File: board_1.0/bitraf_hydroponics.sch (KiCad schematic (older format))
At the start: 40 parts, among them P1 12V_PWR, P10 I2C_4, P11 BUZZ, P12 LDR, P13 TEMP_HUM, P14 PROGRAMMER, P15 LCD, P16 Radio_433, P2 SWITCH_1, P3 SWITCH_2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

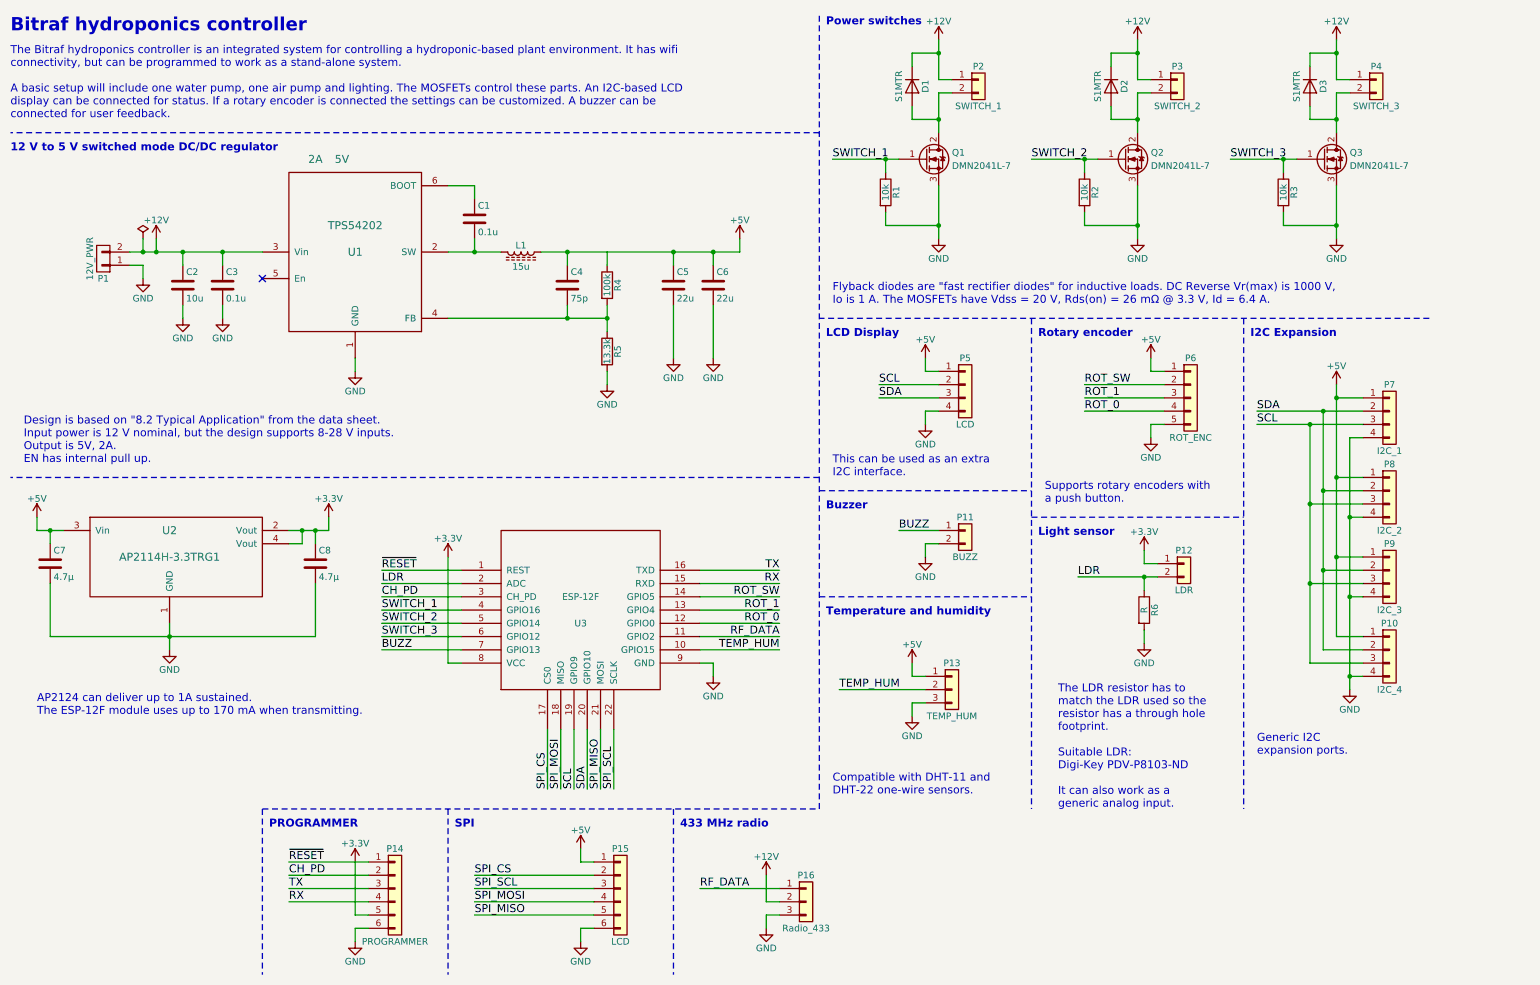
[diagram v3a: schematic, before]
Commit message: schematic: o Changing 12V connector to the same as the rest. o Better label for Radio. o Changing R6 from SMD to THT so it is easier to customize with the LDR. pcb: o Adding copper zones connected to GND on front and back. o Expanding board to 50x100 mm. Moving all connectors onto board.
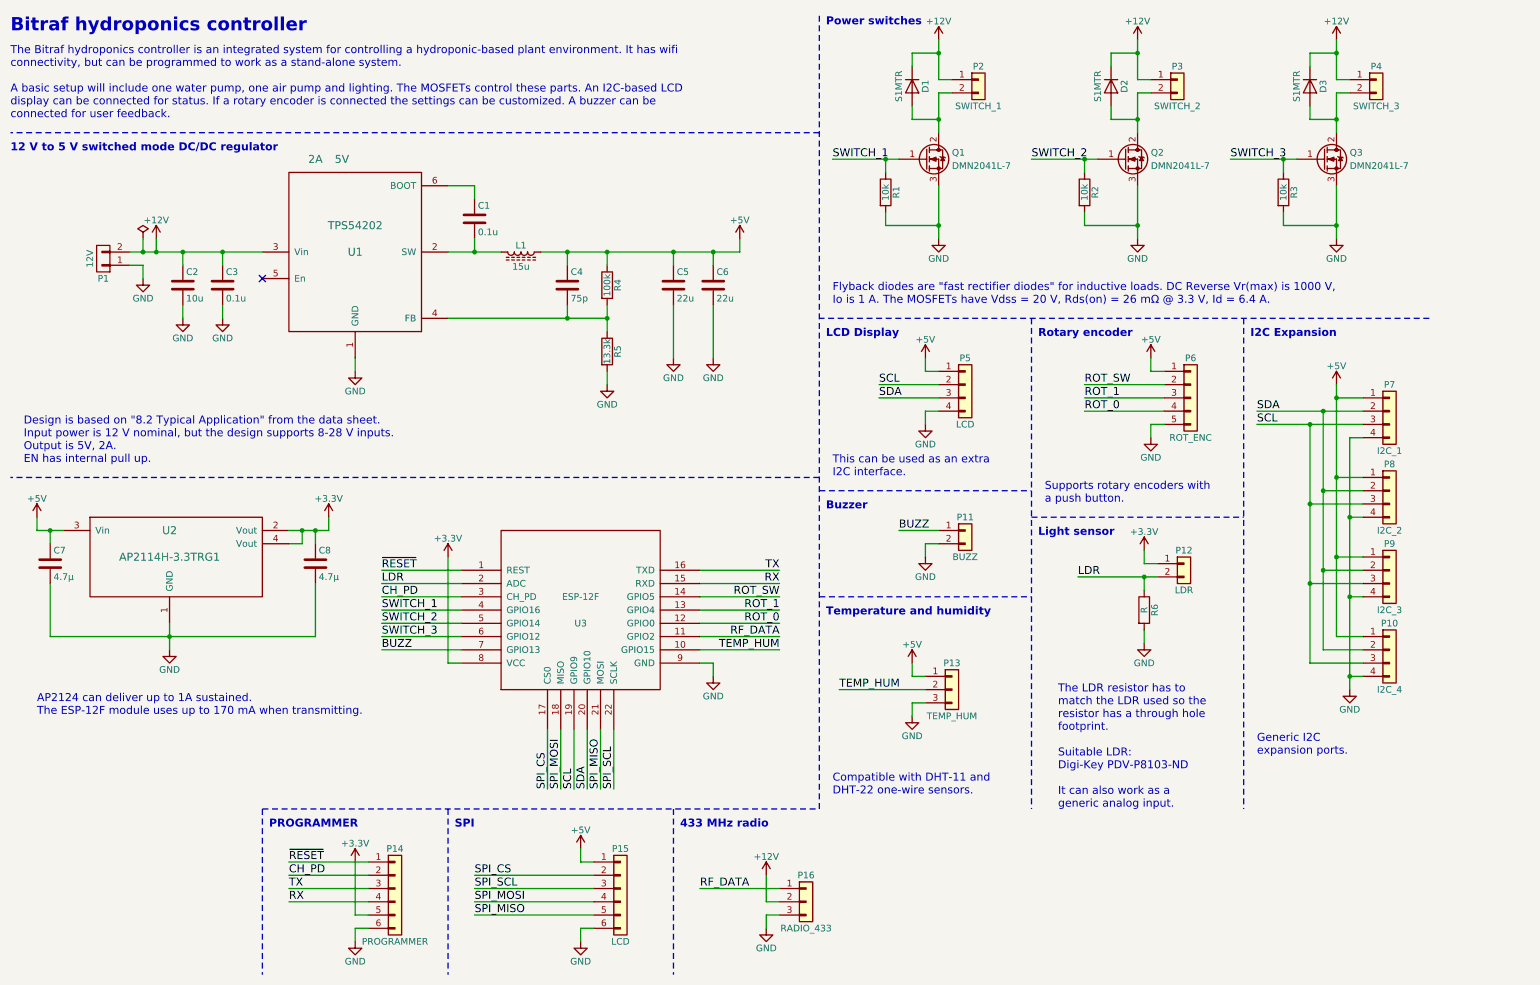
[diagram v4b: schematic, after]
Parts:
- P1: value 12V_PWR -> 12V; footprint Connectors_Terminal_Blocks:TerminalBlock_Pheonix_PT-3.5mm_2pol -> Connectors_Phoenix:PhoenixContact_PTSM0,5_4-HV-2,5_SMD
- P16: value Radio_433 -> RADIO_433
- R6: footprint Resistors_SMD:R_0805 -> Resistors_THT:R_Axial_DIN0207_L6.3mm_D2.5mm_P10.16mm_Horizontal
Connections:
- net +5V: now also R4.1
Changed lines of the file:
@@
 P 6500 7200
 F 0 "P16" H 6500 7400 50  0000 C CNN
-F 1 "Radio_433" H 6500 7000 50  0000 C CNN
+F 1 "RADIO_433" H 6500 7000 50  0000 C CNN
 F 2 "Socket_Strips:Socket_Strip_Straight_1x03_Pitch2.54mm" H 6500 7200 50  0001 C CNN
 F 3 "" H 6500 7200 50  0001 C CNN
@@
 P 1200 2350
 F 0 "P1" H 1200 2500 50  0000 C CNN
-F 1 "12V_PWR" V 1300 2350 50  0000 C CNN
-F 2 "Connectors_Terminal_Blocks:TerminalBlock_Pheonix_PT-3.5mm_2pol" H 1200 2350 50  0001 C CNN
+F 1 "12V" V 1300 2350 50  0000 C CNN
+F 2 "Connectors_Phoenix:PhoenixContact_PTSM0,5_4-HV-2,5_SMD" H 1200 2350 50  0001 C CNN
 F 3 "" H 1200 2350 50  0000 C CNN
 	1    1200 2350
@@
 F 0 "R6" V 9130 5000 50  0000 C CNN
 F 1 "R" V 9050 5000 50  0000 C CNN
-F 2 "Resistors_SMD:R_0805" V 8980 5000 50  0001 C CNN
+F 2 "Resistors_THT:R_Axial_DIN0207_L6.3mm_D2.5mm_P10.16mm_Horizontal" V 8980 5000 50  0001 C CNN
 F 3 "" H 9050 5000 50  0000 C CNN
 	1    9050 5000
@@
 	0    1    1    0
 $EndComp
+Connection ~ 5000 2300
 $EndSCHEMATC

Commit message: switched position on SDA and SCL on the LCD header to match the rest of I2C bus
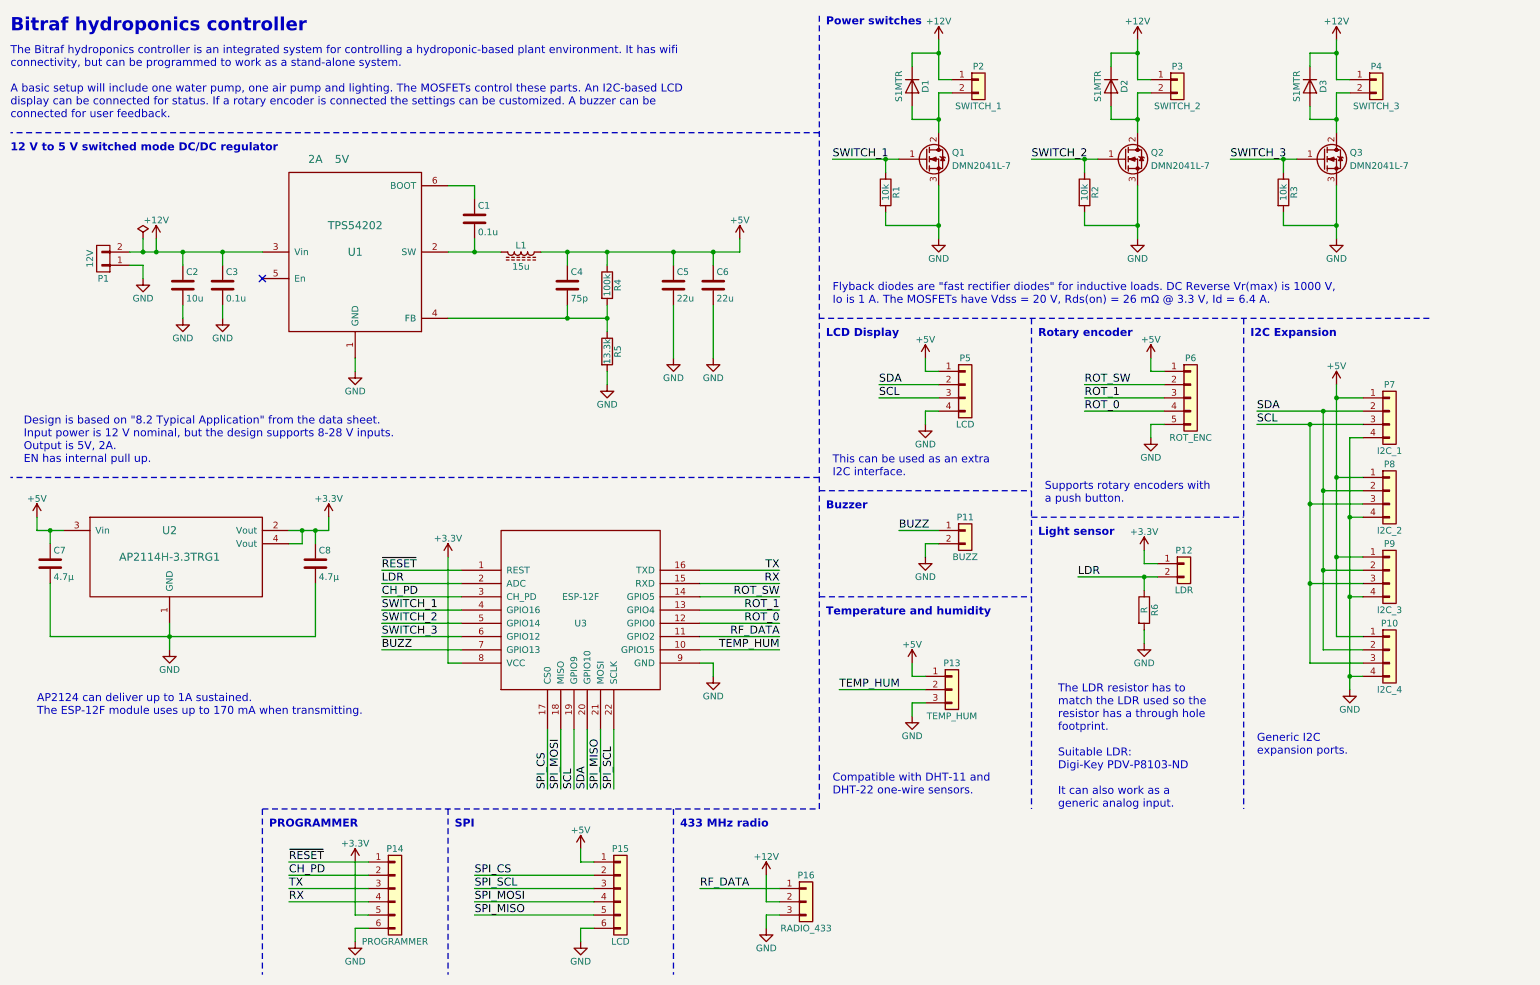
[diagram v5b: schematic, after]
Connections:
- net SCL: now also P5.3 (Pin_3); no longer P5.2 (Pin_2)
- net SDA: now also P5.2 (Pin_2); no longer P5.3 (Pin_3)
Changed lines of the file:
@@
 LIBS:nodemcu
 LIBS:tps54202
-LIBS:ESP8266
 LIBS:ap2114
 LIBS:bitraf_hydroponics-cache
@@
 	1    0    0    -1
 $EndComp
+Text Label 7050 3400 0    60   ~ 0
+SCL
 Text Label 7050 3300 0    60   ~ 0
-SCL
-Text Label 7050 3400 0    60   ~ 0
 SDA
 $Comp
@@
 	7600 1100 7500 1100
 Wire Wire Line
-	7500 1100 7500 1400
+	7500 1100 7500 1300
+Wire Wire Line
+	7500 1300 7500 1400
 Wire Wire Line
 	7500 1000 7600 1000
 Wire Wire Line
-	7500 700  7500 1000
+	7500 700  7500 800
+Wire Wire Line
+	7500 800  7500 1000
 Wire Wire Line
 	7300 1200 7300 1300
@@
 Connection ~ 7500 800
 Wire Wire Line
-	7500 1800 7500 2200
-Wire Wire Line
-	6700 1600 7200 1600
+	7500 1800 7500 2100
+Wire Wire Line
+	7500 2100 7500 2200
+Wire Wire Line
+	6700 1600 7100 1600
+Wire Wire Line
+	7100 1600 7200 1600
 Wire Wire Line
 	7100 1700 7100 1600
@@
 	9100 1100 9000 1100
 Wire Wire Line
-	9000 1100 9000 1400
+	9000 1100 9000 1300
+Wire Wire Line
+	9000 1300 9000 1400
 Wire Wire Line
 	9000 1000 9100 1000
 Wire Wire Line
-	9000 700  9000 1000
+	9000 700  9000 800
+Wire Wire Line
+	9000 800  9000 1000
 Wire Wire Line
 	8800 1200 8800 1300
@@
 Connection ~ 9000 800
 Wire Wire Line
-	9000 1800 9000 2200
-Wire Wire Line
-	8200 1600 8700 1600
+	9000 1800 9000 2100
+Wire Wire Line
+	9000 2100 9000 2200
+Wire Wire Line
+	8200 1600 8600 1600
+Wire Wire Line
+	8600 1600 8700 1600
 Wire Wire Line
 	8600 1700 8600 1600
@@
 	10600 1100 10500 1100
 Wire Wire Line
-	10500 1100 10500 1400
+	10500 1100 10500 1300
+Wire Wire Line
+	10500 1300 10500 1400
 Wire Wire Line
 	10500 1000 10600 1000
 Wire Wire Line
-	10500 700  10500 1000
+	10500 700  10500 800
+Wire Wire Line
+	10500 800  10500 1000
 Wire Wire Line
 	10300 1200 10300 1300
@@
 	10300 900  10300 800
 Wire Wire Line
-	10500 1800 10500 2200
-Wire Wire Line
-	9700 1600 10200 1600
+	10500 1800 10500 2100
+Wire Wire Line
+	10500 2100 10500 2200
+Wire Wire Line
+	9700 1600 10100 1600
+Wire Wire Line
+	10100 1600 10200 1600
 Wire Wire Line
 	10100 1700 10100 1600
@@
 	9200 3500 8600 3500
 Wire Wire Line
-	1400 2300 2400 2300
+	1400 2300 1500 2300
+Wire Wire Line
+	1500 2300 1600 2300
+Wire Wire Line
+	1600 2300 1800 2300
+Wire Wire Line
+	1800 2300 2100 2300
+Wire Wire Line
+	2100 2300 2400 2300
 Wire Wire Line
 	1600 2300 1600 2200
@@
 	7500 4400 7200 4400
 Wire Wire Line
-	8550 4750 9150 4750
+	8550 4750 9050 4750
+Wire Wire Line
+	9050 4750 9150 4750
 Wire Wire Line
 	9050 4750 9050 4850
@@
 	10400 5300 10700 5300
 Wire Wire Line
-	10500 3300 10500 5200
+	10500 3300 10500 3400
+Wire Wire Line
+	10500 3400 10500 4000
+Wire Wire Line
+	10500 4000 10500 4600
+Wire Wire Line
+	10500 4600 10500 5200
 Wire Wire Line
 	10600 5500 10700 5500
@@
 	10400 4100 10700 4100
 Wire Wire Line
-	9900 3600 10700 3600
-Wire Wire Line
-	9900 3500 10700 3500
+	9900 3600 10300 3600
+Wire Wire Line
+	10300 3600 10700 3600
+Wire Wire Line
+	9900 3500 10400 3500
+Wire Wire Line
+	10400 3500 10700 3500
 Wire Wire Line
 	10500 3400 10700 3400
@@
 	8800 1300 9000 1300
 Wire Wire Line
-	3800 2300 4200 2300
-Wire Wire Line
-	4500 2300 6000 2300
+	3800 2300 4000 2300
+Wire Wire Line
+	4000 2300 4200 2300
+Wire Wire Line
+	4500 2300 4700 2300
+Wire Wire Line
+	4700 2300 5000 2300
+Wire Wire Line
+	5000 2300 5500 2300
+Wire Wire Line
+	5500 2300 5800 2300
+Wire Wire Line
+	5800 2300 6000 2300
 Wire Wire Line
 	5000 3200 5000 3300
@@
 	5500 3100 5500 2700
 Wire Wire Line
-	10400 3500 10400 5300
+	10400 3500 10400 4100
+Wire Wire Line
+	10400 4100 10400 4700
+Wire Wire Line
+	10400 4700 10400 5300
 Connection ~ 10400 4100
 Connection ~ 10400 3500
 Connection ~ 10400 4700
 Wire Wire Line
-	10300 3600 10300 5400
+	10300 3600 10300 4200
+Wire Wire Line
+	10300 4200 10300 4800
+Wire Wire Line
+	10300 4800 10300 5400
 Connection ~ 10300 4800
 Connection ~ 10300 4200
@@
 	10600 3700 10700 3700
 Wire Wire Line
-	10600 3700 10600 5600
+	10600 3700 10600 4300
+Wire Wire Line
+	10600 4300 10600 4900
+Wire Wire Line
+	10600 4900 10600 5500
+Wire Wire Line
+	10600 5500 10600 5600
 Wire Notes Line
 	11200 2800 6600 2800
@@
 $EndComp
 Wire Wire Line
-	5000 2700 5000 2900
-Wire Wire Line
-	3800 2800 5000 2800
+	5000 2700 5000 2800
+Wire Wire Line
+	5000 2800 5000 2900
+Wire Wire Line
+	3800 2800 4700 2800
+Wire Wire Line
+	4700 2800 5000 2800
 Wire Wire Line
 	4700 2800 4700 2700
@@
 	700  4300 700  4400
 Wire Wire Line
-	700  4400 900  4400
-Wire Wire Line
-	2600 4400 2900 4400
+	700  4400 800  4400
+Wire Wire Line
+	800  4400 900  4400
+Wire Wire Line
+	2600 4400 2700 4400
+Wire Wire Line
+	2700 4400 2800 4400
+Wire Wire Line
+	2800 4400 2900 4400
 Wire Wire Line
 	2900 4400 2900 4300
@@
 $EndComp
 Wire Wire Line
-	1700 5100 1700 5300
+	1700 5100 1700 5200
+Wire Wire Line
+	1700 5200 1700 5300
 $Comp
 L C C7
@@
 	800  4800 800  5200
 Wire Wire Line
-	800  5200 2800 5200
+	800  5200 1700 5200
+Wire Wire Line
+	1700 5200 2800 5200
 Connection ~ 1700 5200
 $Comp
